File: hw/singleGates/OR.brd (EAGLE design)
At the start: 7.1 x 12.5 mm, 8 parts, among them Q1 BC817, Q2 BC817, Q3 BC817

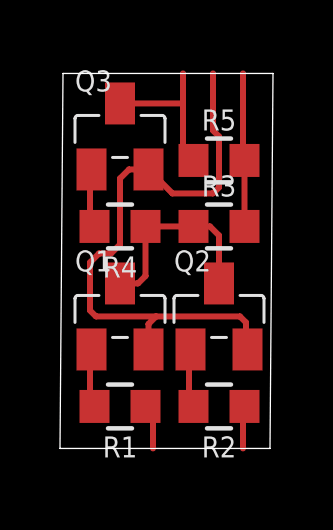
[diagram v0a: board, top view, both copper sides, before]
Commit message: removed unecessary border
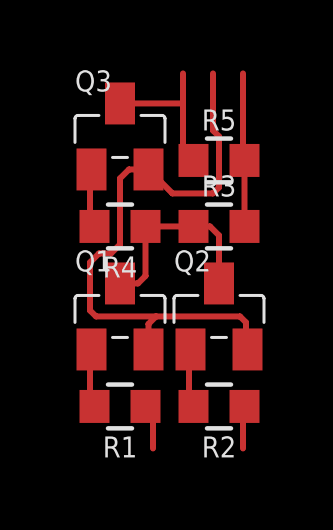
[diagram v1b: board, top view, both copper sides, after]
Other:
- board outline removed
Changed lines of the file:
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@@
 <board>
 <plain>
-<wire x1="-0.1" y1="0" x2="0" y2="12.5" width="0" layer="20"/>
-<wire x1="0" y1="12.5" x2="7" y2="12.5" width="0" layer="20"/>
-<wire x1="7" y1="12.5" x2="6.9" y2="0" width="0" layer="20"/>
-<wire x1="6.9" y1="0" x2="-0.1" y2="0" width="0" layer="20"/>
 <wire x1="0" y1="0" x2="7" y2="0" width="0.2" layer="22" style="shortdash"/>
 <wire x1="7" y1="0" x2="7" y2="12.5" width="0.2" layer="22" style="shortdash"/>
